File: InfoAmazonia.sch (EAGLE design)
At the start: 78 parts, among them IC1 LM2662, IC2 ADAFRUIT FONA, IC3 MIC29302AWD, IC4 4050D, IC5 TL032C, IC6 CA3140AM Z, IC7 TL081BCDG4, IC8 SHT20, IC9 NE555, J1 BNCPTH, J2 BNCPTH, J3 BNCPTH, U1 ARDUINO-MEGAPRO, U2 MPL3115A2, U3 USD-SOCKETNEW, U4 ALS-PT19

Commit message: [INFOA-26]
- Mudanças de conector JST PH
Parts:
- removed JP13: (no value), InfoAmazonia:PINHD-1X3180
- removed R17: 4k7, InfoAmazonia:R-EU_R0603
- added JP14, JP15, JP16, JP17: (no value), InfoAmazonia:M04JST-PTH-VERT
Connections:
- new net +12V: C4.+, C5.+, IC3.IN, U1.VIN
- new net A14: JP14.1, U1.A14
- new net A15: JP14.2, U1.A15
- new net RX2: JP17.1, U1.17(RX2)
- new net RX3: JP16.1, U1.15(RX3)
- new net TX2: JP17.2, U1.16(TX2)
- new net TX3: JP16.2, U1.14(TX3)
- net +5V: now also JP14.3, JP15.3, JP16.3, JP17.3; no longer C4.+, C5.+, IC3.IN, JP13.1, R17.1
- net FREQ_SENSOR: now also U1.47
- net GND: now also JP14.4, JP15.4, JP16.4, JP17.4; no longer JP13.3
- net SCL: now also JP15.1
- net SDA: now also JP15.2
- net TEMP_SENSOR: no longer JP13.2, R17.2

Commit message: - Mudancas no silkscreen da placa
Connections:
- new net +VEC: C31.1, IC9./RES, IC9.VCC+, JP3.3
- new net +VORP: C14.1, C17.1, IC5P.V+, JP7.3
- new net +VPH: C12.1, C22.1, C23.1, C9.1, IC6.+VS, IC7.+VS, JP1.3
- new net -VORP: C25.1, C27.1, IC5P.V-, JP7.2, R9.2
- new net -VPH: C15.1, C18.1, C24.1, C26.1, IC6.-VS, IC7.-VS, JP1.2, R10.2
- net +5V: no longer C12.1, C14.1, C17.1, C22.1, C23.1, C31.1, C9.1, IC5P.V+, IC6.+VS, IC7.+VS, IC9./RES, IC9.VCC+, JP1.3, JP3.3, JP7.3
- net -5V: no longer C15.1, C18.1, C24.1, C25.1, C26.1, C27.1, IC5P.V-, IC6.-VS, IC7.-VS, JP1.2, JP3.2, JP7.2, R10.2, R9.2

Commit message: - Ajustes depois do prototipo
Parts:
- C32: value 1uF -> 100nF

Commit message: - Mudanças bem minimas (Valores de capacitor por exemplo)
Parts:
- C4, C5: value 220uF -> 47uF
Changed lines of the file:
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@@
 <part name="R1" library="InfoAmazonia" deviceset="R-EU_" device="R0603" value="43k"/>
 <part name="GND9" library="InfoAmazonia" deviceset="GND" device=""/>
-<part name="C5" library="InfoAmazonia" deviceset="CPOL-EU" device="UD6,3-5,8" value="220uF"/>
-<part name="C4" library="InfoAmazonia" deviceset="CPOL-EU" device="UD6,3-5,8" value="220uF"/>
+<part name="C5" library="InfoAmazonia" deviceset="CPOL-EU" device="UD6,3-5,8" value="47uF"/>
+<part name="C4" library="InfoAmazonia" deviceset="CPOL-EU" device="UD6,3-5,8" value="47uF"/>
 <part name="C6" library="InfoAmazonia" deviceset="CPOL-EU" device="UD6,3-5,8" value="220uF"/>
 <part name="C7" library="InfoAmazonia" deviceset="CPOL-EU" device="UD6,3-5,8" value="220uF"/>

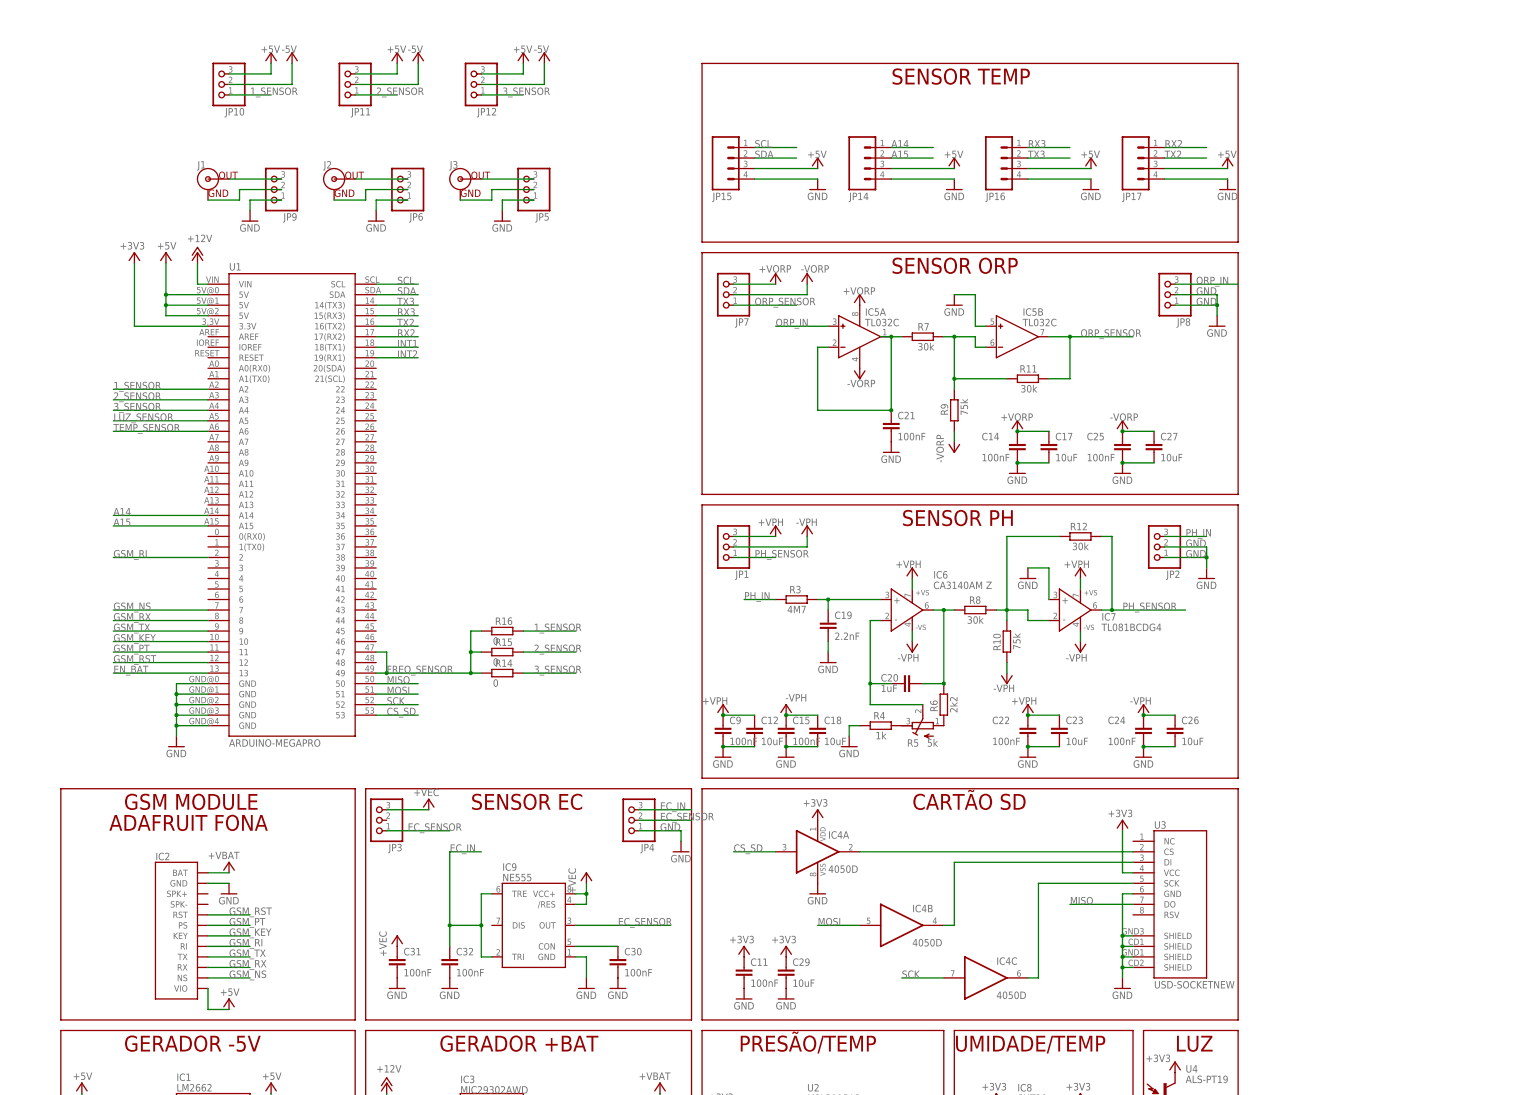
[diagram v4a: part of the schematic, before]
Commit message: - Agora os modulos tem tamanho definido via componente nas bibliotecas
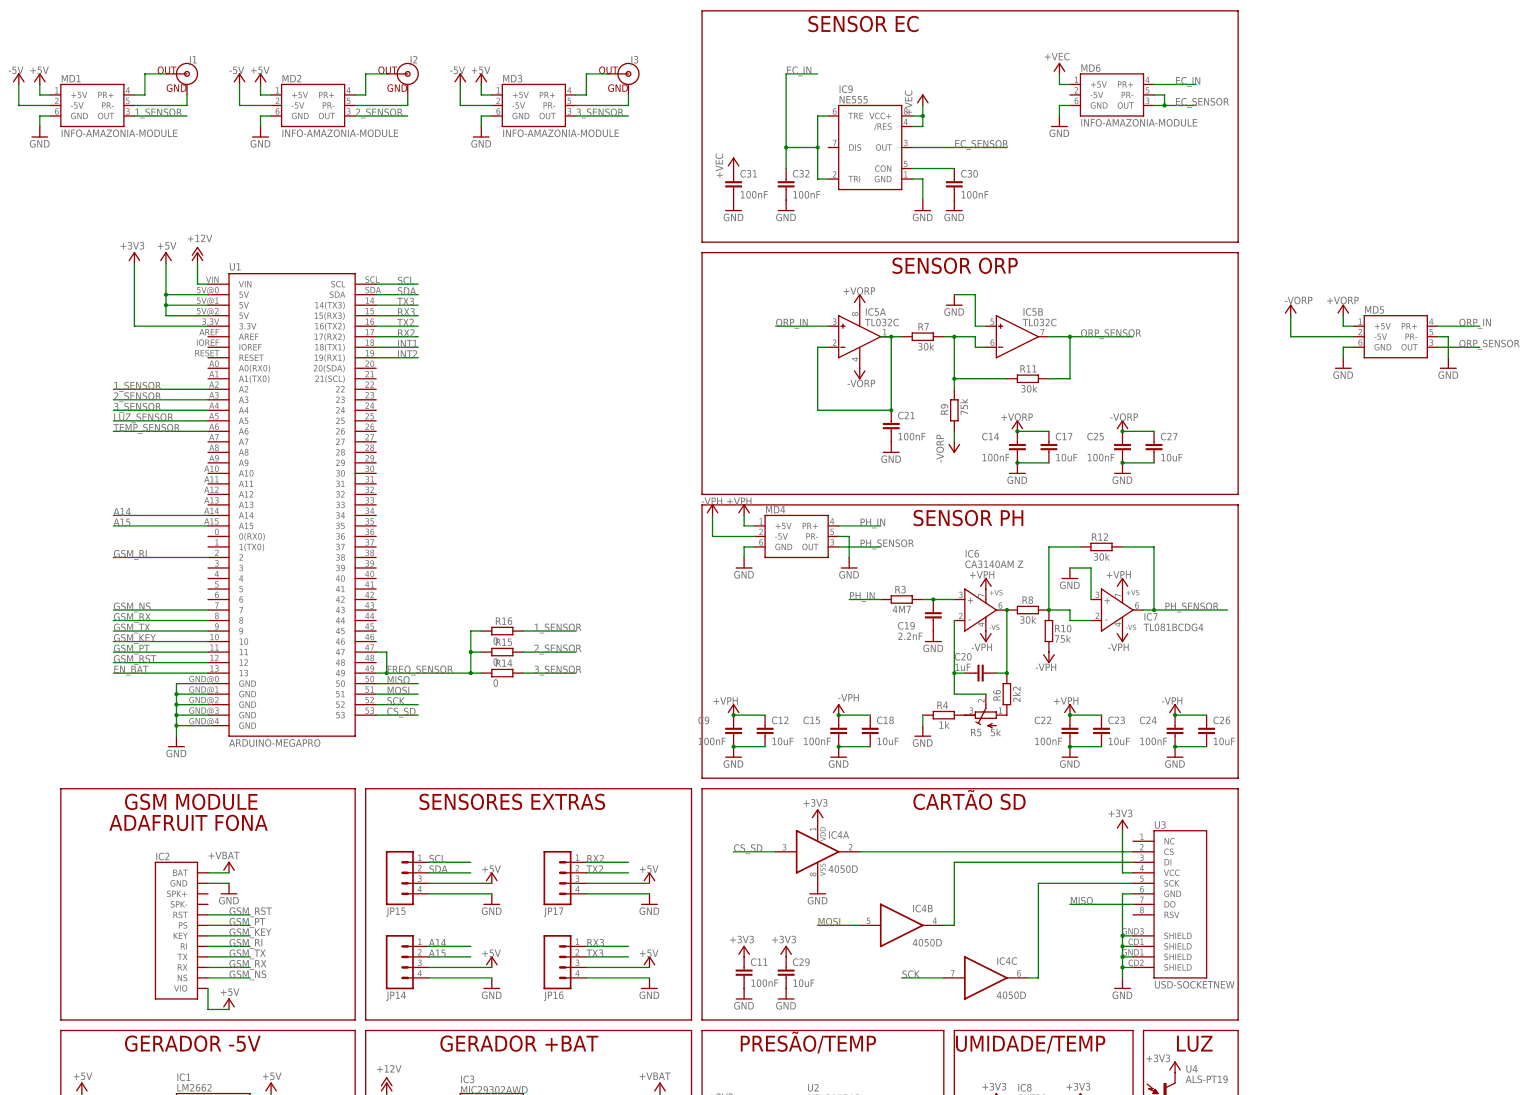
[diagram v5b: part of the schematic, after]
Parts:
- removed JP1, JP10, JP11, JP12, JP2, JP3, JP4, JP5, JP6, JP7, JP8, JP9: (no value), InfoAmazonia:PINHD-1X3180
- added MD1, MD2, MD3, MD4, MD5, MD6: INFO-AMAZONIA-MODULE, InfoAmazonia:INFO-AMAZONIA-MODULE
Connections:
- net +5V: now also MD1.+5V, MD2.+5V, MD3.+5V; no longer JP10.3, JP11.3, JP12.3
- net +VEC: now also MD6.+5V; no longer JP3.3
- net +VORP: now also MD5.+5V; no longer JP7.3
- net +VPH: now also MD4.+5V; no longer JP1.3
- net -5V: now also MD1.-5V, MD2.-5V, MD3.-5V; no longer JP10.2, JP11.2, JP12.2
- net -VORP: now also MD5.-5V; no longer JP7.2
- net -VPH: now also MD4.-5V; no longer JP1.2
- net 1_SENSOR: now also MD1.OUT; no longer JP10.1
- net 2_SENSOR: now also MD2.OUT; no longer JP11.1
- net 3_SENSOR: now also MD3.OUT; no longer JP12.1
- net EC_IN: now also MD6.PR+; no longer JP4.3
- net EC_SENSOR: now also MD6.OUT, MD6.PR-; no longer JP3.1, JP4.2
- net GND: now also MD1.GND, MD2.GND, MD3.GND, MD4.GND, MD4.PR-, MD5.GND, MD5.PR-, MD6.GND; no longer JP2.1, JP2.2, JP4.1, JP5.1, JP6.1, JP8.1, JP8.2, JP9.1
- net N$1: now also J1.GND, MD1.PR-; no longer J1.OUT, JP9.3
- net N$11: now also J2.GND, MD2.PR-; no longer J2.OUT, JP6.3
- net N$12: now also J2.OUT, MD2.PR+; no longer J2.GND, JP6.2
- net N$13: now also J3.GND, MD3.PR-; no longer J3.OUT, JP5.3
- net N$22: now also J3.OUT, MD3.PR+; no longer J3.GND, JP5.2
- net N$9: now also J1.OUT, MD1.PR+; no longer J1.GND, JP9.2
- net ORP_IN: now also MD5.PR+; no longer JP8.3
- net ORP_SENSOR: now also MD5.OUT; no longer JP7.1
- net PH_IN: now also MD4.PR+; no longer JP2.3
- net PH_SENSOR: now also MD4.OUT; no longer JP1.1
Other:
- note added: "SENSORES EXTRAS"
- note removed: "SENSOR TEMP"
- moved on the sheet: C12, C15, C18, C19, C20, C22, C23, C24, C26, C30, C31, C32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

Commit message: - Mudanca no pino rx/tx do fona
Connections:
- removed net GSM_RX: IC2.RX, U1.8
- removed net GSM_TX: IC2.TX, U1.9
- net RX2: now also IC2.TX; no longer JP17.1
- net TX2: now also IC2.RX; no longer JP17.2
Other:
- moved on the sheet: JP14, JP15, JP16, JP17

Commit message: -
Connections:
- removed net TEMP_SENSOR: U1.A6
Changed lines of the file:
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@@
-</segment>
-</net>
-<net name="TEMP_SENSOR" class="0">
-<segment>
-<pinref part="U1" gate="G$1" pin="A6"/>
-<wire x1="-2.54" y1="55.88" x2="-25.4" y2="55.88" width="0.1524" layer="91"/>
-<label x="-25.4" y="55.88" size="1.778" layer="95"/>
 </segment>
 </net>

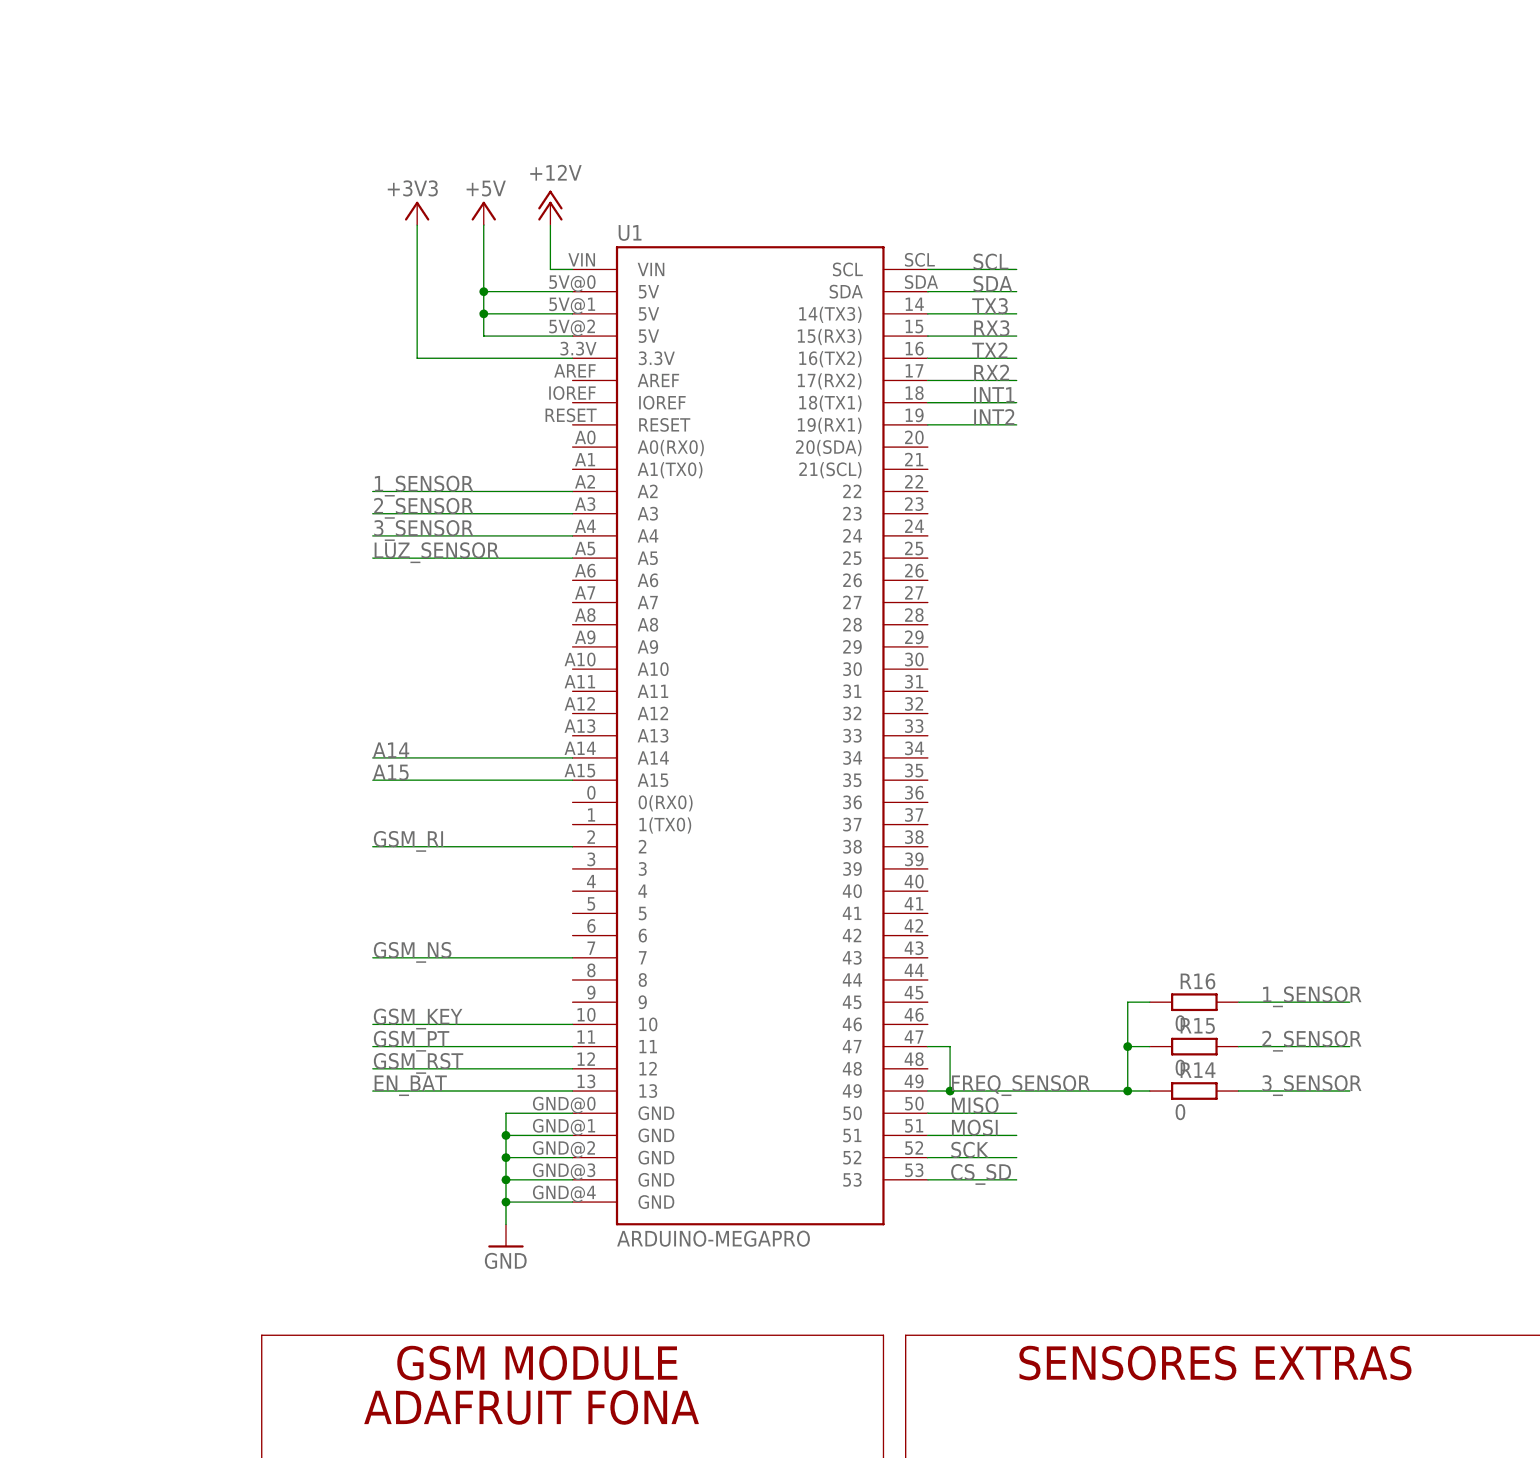
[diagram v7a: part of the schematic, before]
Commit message: - Commit antes de tentar transferir os sensores de temp/luz/presao para a lateral direita
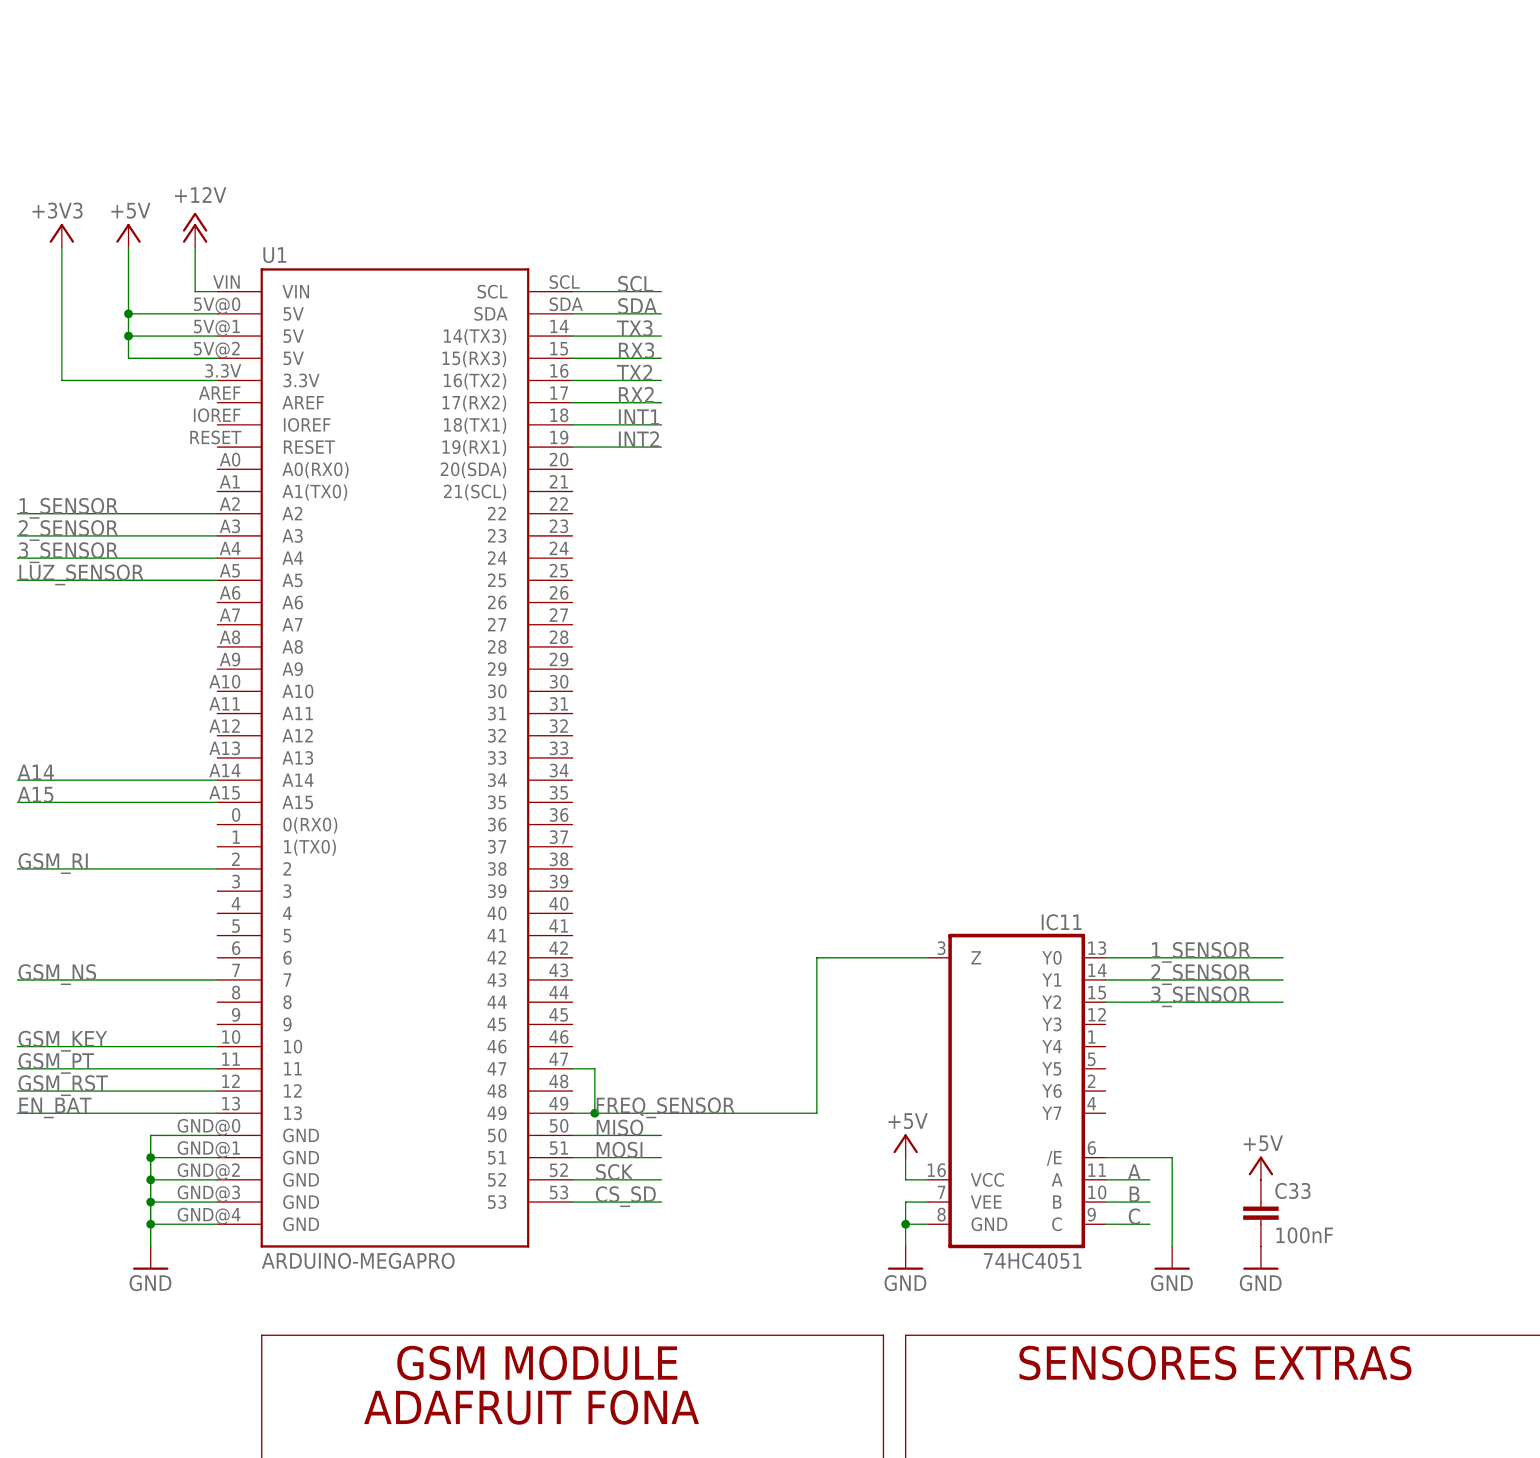
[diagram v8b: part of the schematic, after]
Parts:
- removed R14, R15, R16: 0, InfoAmazonia:R-EU_R0603
- added C33: 100nF, InfoAmazonia:C-EUC0603
- added IC11: 74HC4051, InfoAmazonia:4051PW
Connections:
- new net A: IC11.A
- new net B: IC11.B
- new net C: IC11.C
- net +5V: now also C33.1, IC11.VCC
- net 1_SENSOR: now also IC11.Y0; no longer R16.2
- net 2_SENSOR: now also IC11.Y1; no longer R15.2
- net 3_SENSOR: now also IC11.Y2; no longer R14.2
- net FREQ_SENSOR: now also IC11.Z; no longer R14.1, R15.1, R16.1
- net GND: now also C33.2, IC11./E, IC11.GND, IC11.VEE
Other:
- moved on the sheet: U1
